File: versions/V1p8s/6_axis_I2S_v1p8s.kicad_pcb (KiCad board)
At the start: 2 copper layers, 134 x 132 mm, 96 parts, among them J1 2 Pos, J10 8S, J11 JTAG, J12 2 Pos, J13 8S, J14 8S, J15 2 Pos, J16 8S, J17 8S, J18 6S, J19 2 Pos, J2 8S, J20 8S, J21 8S, J22 3P, J23 3P, J24 3P, J25 6S, J26 2 Pos, J27 8S, J28 8S, J3 8S, J4 19S, J5 ESP32_DEVKITC_01-19, J6 ESP32_DEVKITC_20-38, J7 19S, J8 2 Pos, J9 8S, U1 74AHCT595, U2 74AHCT595, U3 74AHCT595, U4 74AHCT595, U5 TPS54360

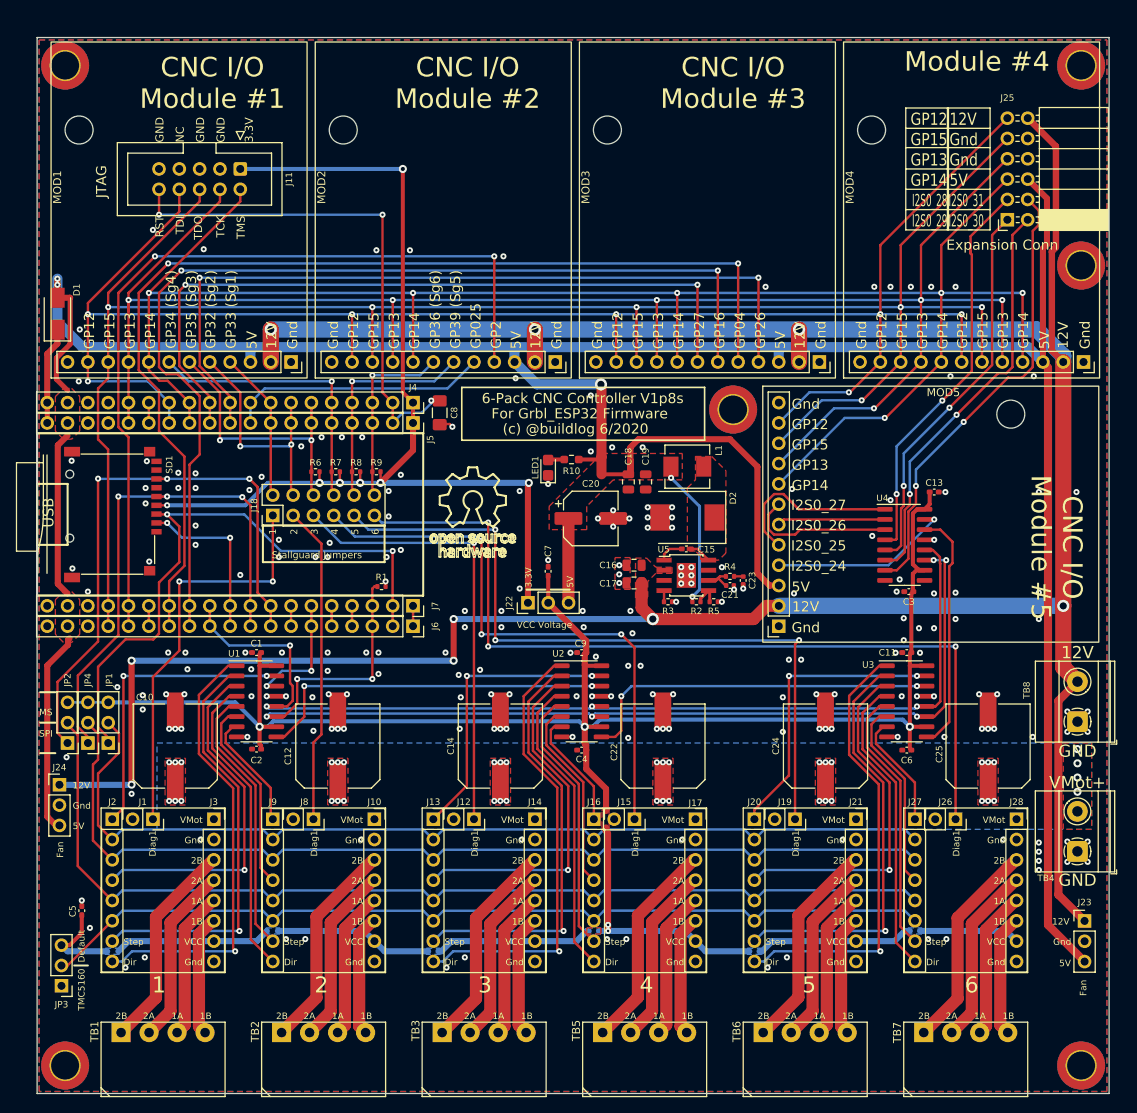
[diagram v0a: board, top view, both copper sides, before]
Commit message: layout changes, screw hole placement changes, generate gerbers
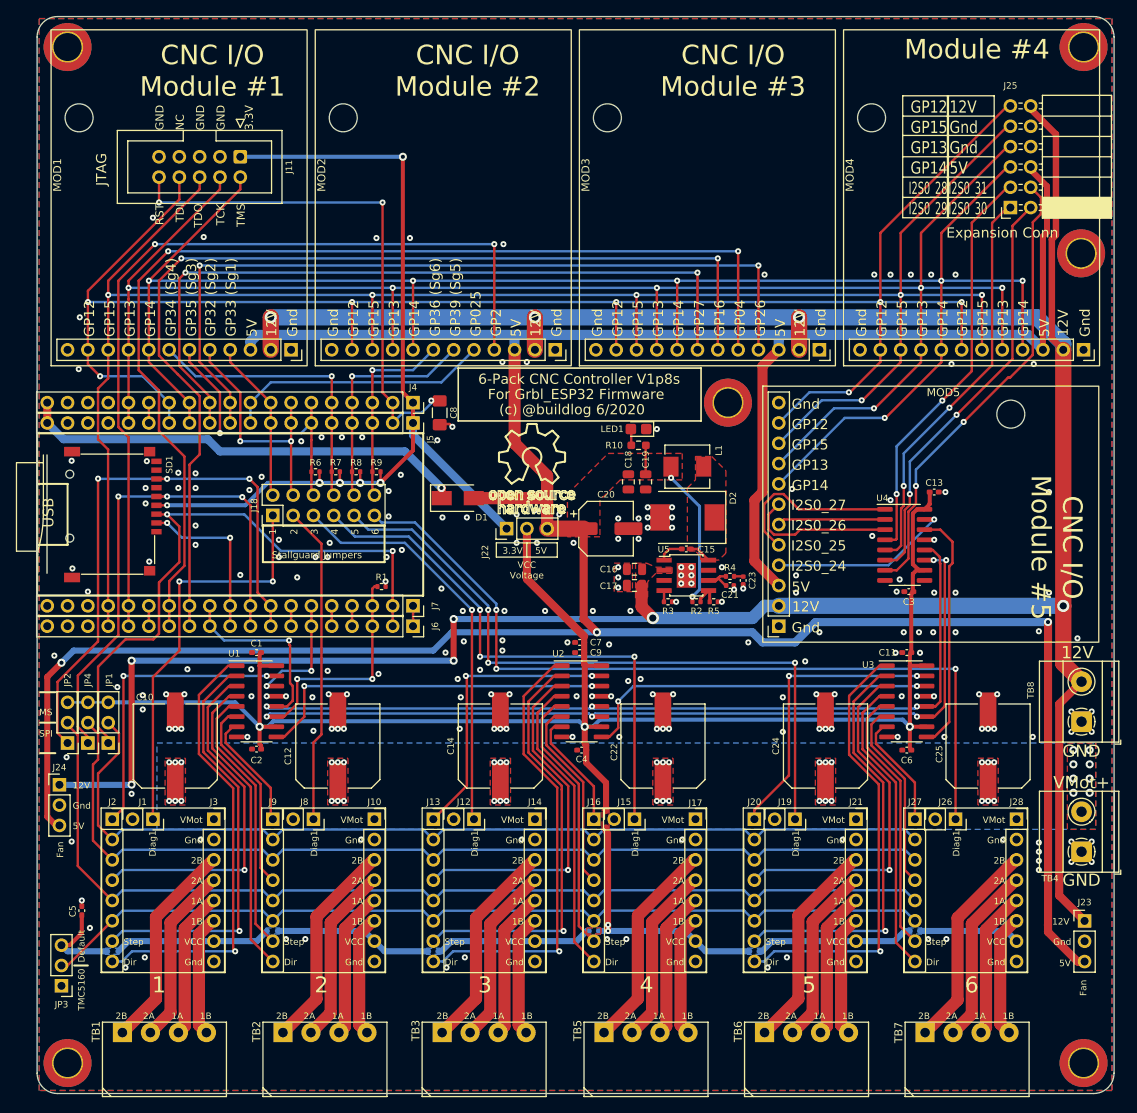
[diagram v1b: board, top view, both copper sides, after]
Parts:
- moved D1 55.1 mm to (133.9, 97.0), turned to 0 degrees
- moved LED1 12.3 mm to (156.5, 88.4), turned to 180 degrees
- moved C7 9.72 mm to (149.1, 115.1), turned to 0 degrees
- moved J22 9.65 mm to (140.0, 100.8)
- moved R10 8.57 mm to (156.5, 90.4)
- moved MH2 2.33 mm to (212.1, 40.6)
- moved MH3 2.33 mm to (85.1, 40.6)
- moved C20 2.29 mm to (152.4, 100.8)
- moved J25 1.57 mm to (202.9, 60.7)
- moved J11 1.52 mm to (106.7, 54.4)
- moved MH6 1.52 mm to (211.8, 66.4)
- moved MOD1 1.52 mm to (113.0, 78.5)
- moved MOD2 1.52 mm to (146.1, 78.5)
- moved MOD3 1.52 mm to (179.1, 78.5)
- moved MOD4 1.52 mm to (212.1, 78.5)
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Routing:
- net Net-(D1-Pad1): track 12.2 -> 56.5 mm, vias 0 -> 1
- net +5V: track 399.3 -> 428.1 mm
- net +3V3: track 130.1 -> 116.3 mm, vias 7 -> 6
- net VCC: track 337.6 -> 344.4 mm
- net /B_DIAG1: track 92.8 -> 86.5 mm
- net /C_DIAG1: track 110.1 -> 104.1 mm
- net /Z_DIAG1: track 56.0 -> 51.0 mm
- net /A_DIAG1: track 73.0 -> 68.8 mm
- net /GPIO15: track 243.1 -> 246.6 mm
- net /GPIO14: track 224.7 -> 227.5 mm
- net /GPIO12: track 222.6 -> 224.7 mm
- net /GPIO13: track 220.7 -> 222.6 mm
- net /X_LIMIT: track 18.8 -> 20.4 mm
- net /GPIO26: track 100.1 -> 101.7 mm
- net /GPIO4: track 133.6 -> 135.1 mm
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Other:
- board size 134 x 132 mm -> 134.6 x 134.6 mm
- board text added: "12-48V"
- board text removed: "12-24V"
